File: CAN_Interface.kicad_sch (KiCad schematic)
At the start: 16 parts, among them CN2 BM04B-ACHSS, U1 TPSM82903, U2 TPS2117DRL, U7 TCAN1057AVDRBRQ1

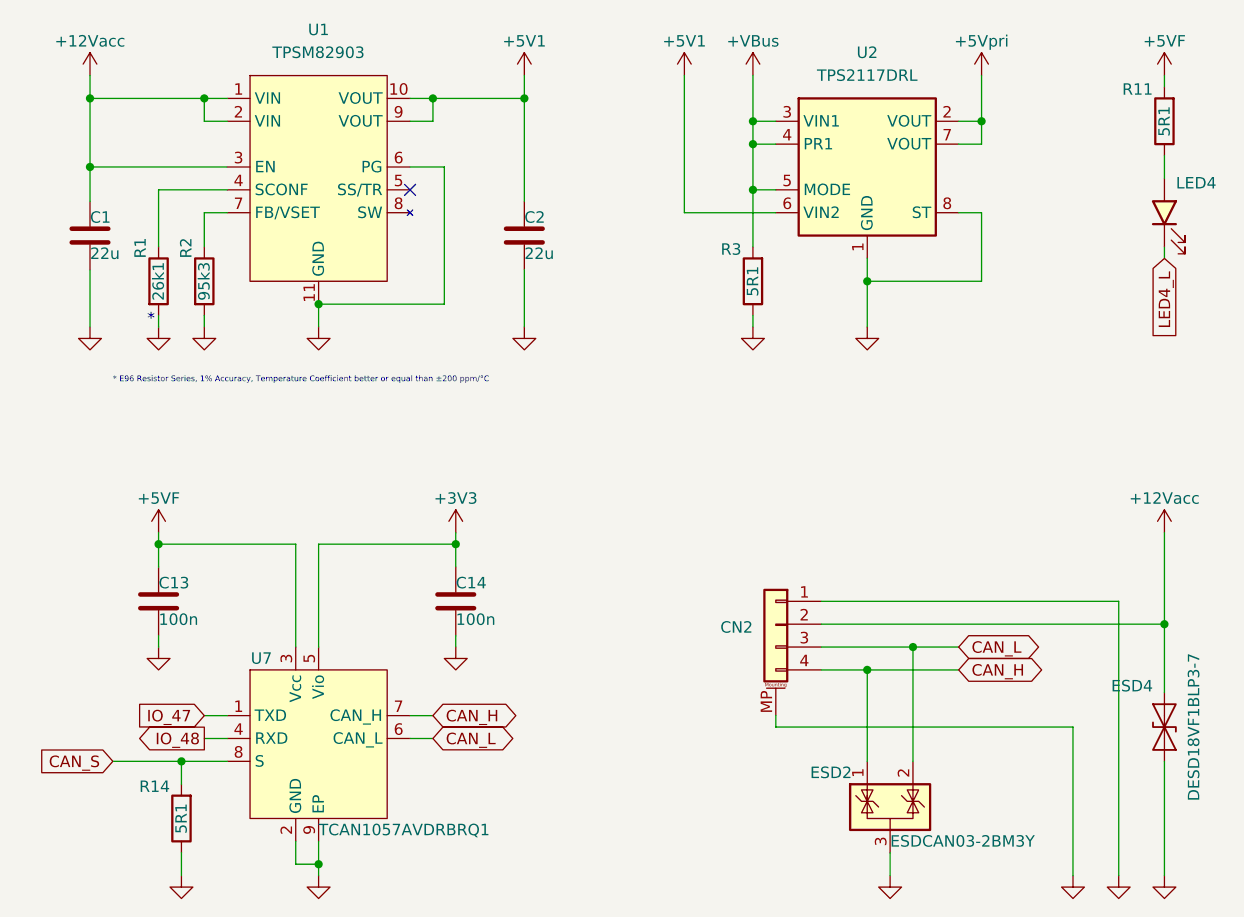
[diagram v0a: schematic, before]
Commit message: successful 1st pass, but I want to try some new bus'ing techniques to clean up the routing
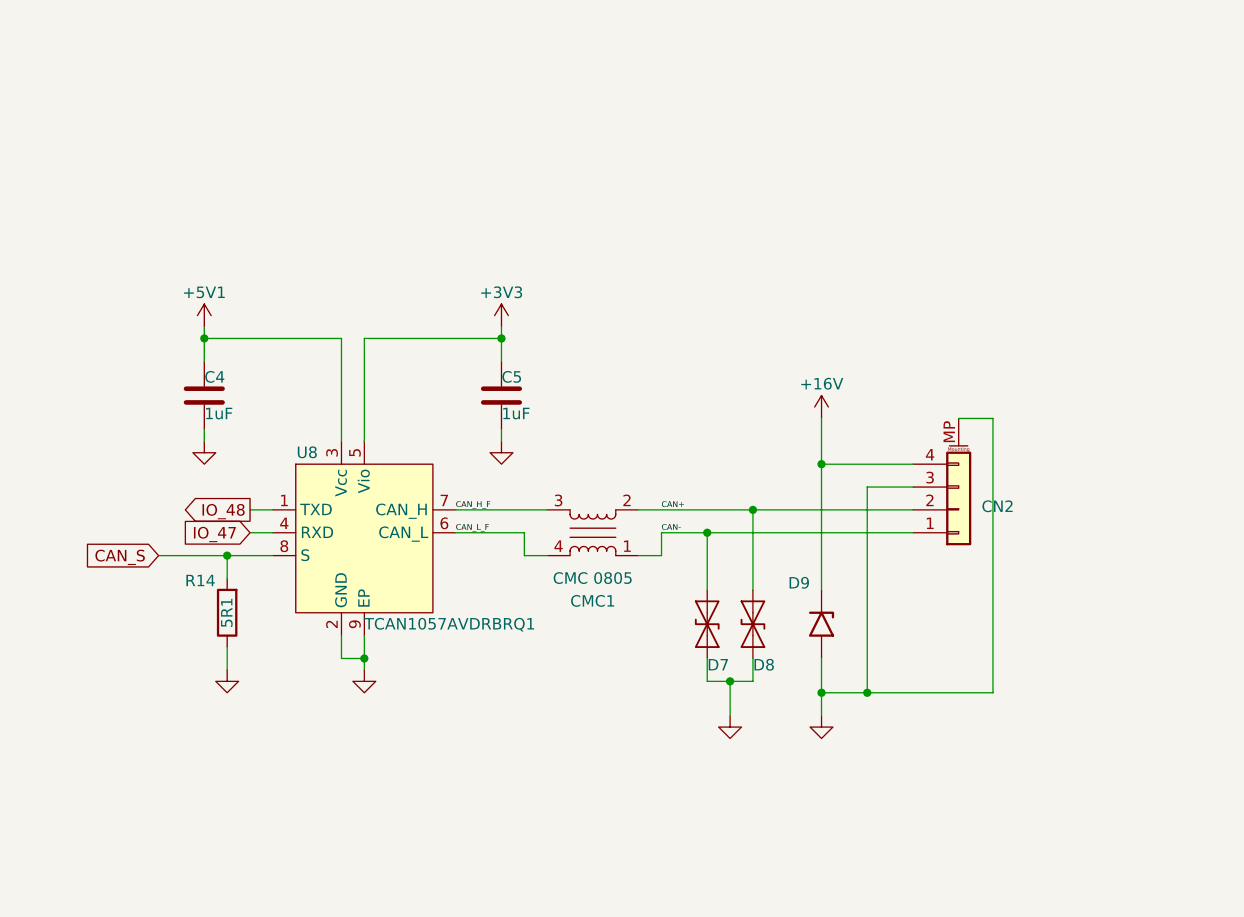
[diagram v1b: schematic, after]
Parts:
- removed C1, C2: 22u, Capacitors:C0805_Dense, symbol Device:C
- removed C13, C14: 100n, Capacitors:C0201_Dense, symbol Device:C
- removed ESD2: ESDCAN03-2BM3Y, Personal_FootprintLibrary:DFN1110-3, symbol PersonalSchematicSymbolLibrary:ESDCAN03-2BM3Y
- removed ESD4: DESD18VF1BLP3-7, Personal_FootprintLibrary:DSN0603-2, symbol PersonalSchematicSymbolLibrary:PESD5V0X1BCSF
- removed LED4: Red, Personal_FootprintLibrary:LED_0201-2, symbol PersonalSchematicSymbolLibrary:LED_Red
- removed R1: 26k1, Resistors:R0201_Nominal, symbol Device:R
- removed R11, R3: 5R1, Resistors:R0201_Nominal, symbol Device:R
- removed R2: 95k3, Resistors:R0201_Nominal, symbol Device:R
- removed U1: TPSM82903, Personal_FootprintLibrary:uSIP-11_3.0x2.8, symbol PersonalSchematicSymbolLibrary:TPSM82903
- removed U2: TPS2117DRL, Personal_FootprintLibrary:SOT5x3, symbol PersonalSchematicSymbolLibrary:TPS2117DRL
- added C4, C5: 1uF, Capacitors:C0201_Dense, symbol Device:C
- added CMC1: CMC 0805, Personal_FootprintLibrary:CMC_0805, symbol PersonalSchematicSymbolLibrary:Choke_CommonMode_TDK_ACM0805
- added D7, D8: PESD24VF1BL-Q, Personal_FootprintLibrary:DFN1006-2, symbol PersonalSchematicSymbolLibrary:PESD24VF1BBL-Q
- added D9: VESD16C1-HD1HG3-08, Personal_FootprintLibrary:DFN1006-2, symbol PersonalSchematicSymbolLibrary:TVS_Unidirectional
- R14: footprint Resistors:R0201_Nominal -> Resistors:R0201_Dense
- renumbered U7 to U8
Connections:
- net +5VF is gone; now on net +5V1: U8.3 (Vcc)
- net +3V3: now also C5.1
- net +5V1: now also C4.1
- net GND: now also CN2.3 (CAN_L), C4.2, C5.2, D7.2 (A2), D8.2 (A2), D9.2 (A2); no longer CN2.1 (GND)
- net IO_47: now also U8.4 (RXD); no longer U8.1 (TXD)
- net IO_48: now also U8.1 (TXD); no longer U8.4 (RXD)
- net +12Vacc renamed CAN+
- net CAN+: now also CMC1.2, D8.1 (A1)
- net CAN_H renamed +16V
- net +16V: now also D9.1 (A1); no longer U8.7 (CAN_H)
- net CAN_L renamed CAN_L_F
- net CAN_L_F: now also CMC1.4; no longer CN2.3 (CAN_L)
- new net CAN-: CMC1.1, CN2.1 (GND), D7.1 (A1)
- new net CAN_H_F: CMC1.3, U8.7 (CAN_H)
- no-connect marks 1 -> 0
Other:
- note removed: "*"
- note removed: "* E96 Resistor Series, 1% Accuracy, Temperature Coefficient better or equal than ±200 ppm/°C"
- moved on the sheet: CN2, R14, U8

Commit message: Update CAN_Interface.kicad_sch, ESP32-S3 Pico D1.kicad_dru, ESP32-S3 Pico D1.kicad_pcb, and 5 more files reroute completed
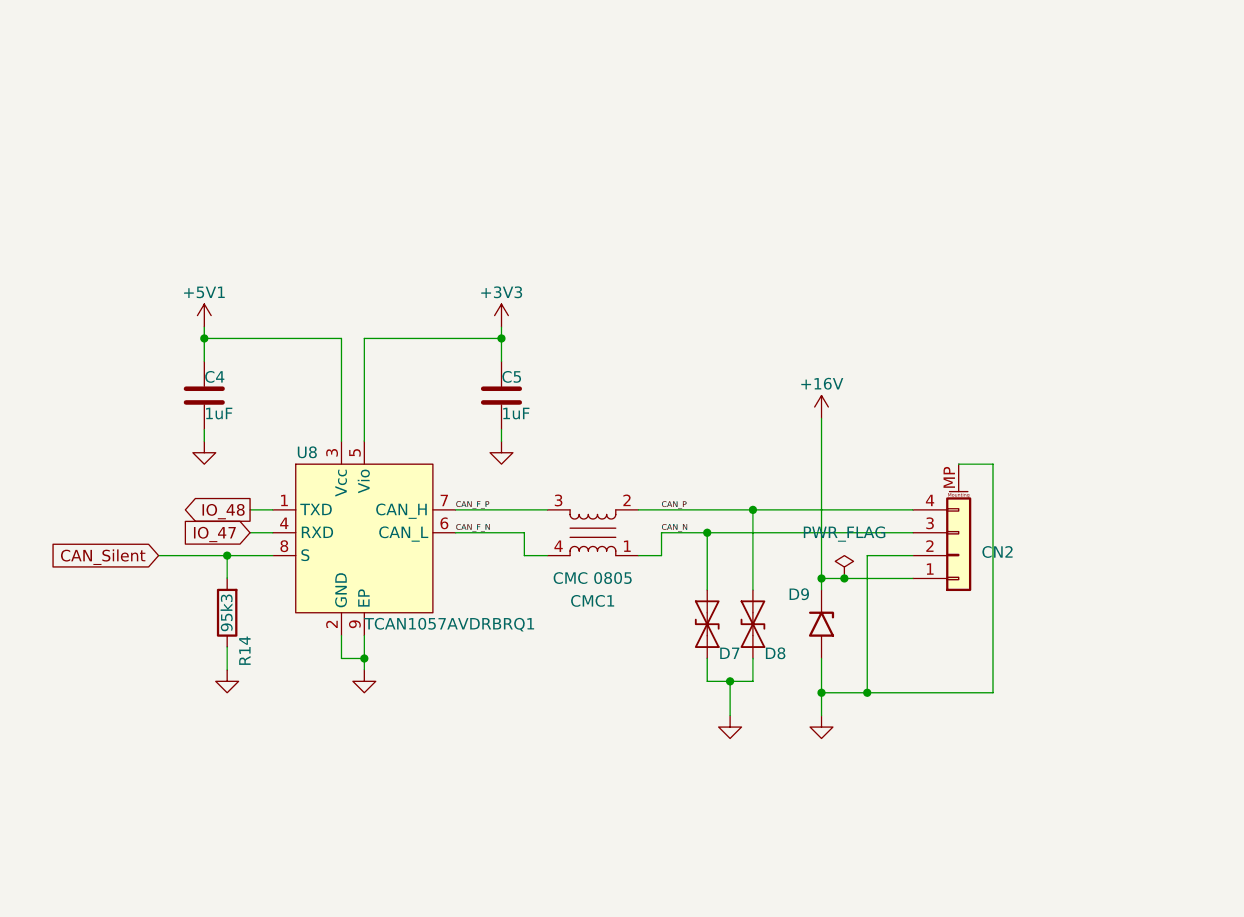
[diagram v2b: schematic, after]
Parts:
- CN2: LCSC C46772640, C5246838, C5308725 -> C46772640; Manufacturer JST -> XUNPU; Manufacturer (alt) Xunpu -> (none); Manufacturer Part Number BM04B-ACHSS-A-GAN-TF(LF)(SN), BM04B-ACHSS-A-GAN-ETF(LF)(SN) -> WAFER-ACH1.2-4PWB; Manufacturer Part Number (alt) WAFER-ACH1.2-4PWB -> (none)
- D7, D8: value PESD24VF1BL-Q -> ESDSLC24VLB-TP; Distributor Link 1 https://www.digikey.com/en/products/detail/nexperia-usa-inc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 -> https://www.digikey.com/en/products/detail/mcc-micro-commer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; Distributor Link 2 https://www.mouser.com/ProductDetail/Nexperia/PESD24VF1BBL-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 -> https://www.mouser.com/ProductDetail/Micro-Commercial-Compo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; LCSC C22465859 -> C7463931; Manufacturer Nexperia -> MCC(Micro Commercial Components); Manufacturer Part Number PESD24VF1BBL-Q -> ESDSLC24VLB-TP
- D9: value VESD16C1-HD1HG3-08 -> D15V0H1U2LP-7B; Distributor Link 1 https://www.digikey.com/en/products/detail/vishay-general-s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 -> https://www.digikey.com/en/products/detail/diodes-incorpora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; Distributor Link 2 https://www.mouser.com/ProductDetail/Vishay-General-Semicon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 -> https://www.mouser.com/ProductDetail/Diodes-Incorporated/D1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; LCSC C3703781 -> C1973850; Manufacturer Vishay -> Diodes Incorporated; Manufacturer Part Number VESD16C1-HD1HG3-08 -> D15V0H1U2LP-7B
- R14: value 5R1 -> 95k3; Distributor Link 2 https://www.mouser.com/ProductDetail/Royalohm/PF01WMF5100TE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 -> https://www.mouser.com/ProductDetail/Royalohm/0201WMF9532TE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; LCSC C50670526 -> C423395; Manufacturer Part Number PF01WMF510KTEE -> 0201WMF9532TEE
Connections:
- net +16V: now also CN2.1 (GND); no longer CN2.4 (CAN_H)
- net GND: now also CN2.2 (+12V); no longer CN2.3 (CAN_L)
- net CAN+ renamed CAN_P
- net CAN_P: now also CN2.4 (CAN_H); no longer CN2.2 (+12V)
- net CAN- renamed CAN_N
- net CAN_N: now also CN2.3 (CAN_L); no longer CN2.1 (GND)
- net CAN_H_F renamed CAN_F_P
- net CAN_L_F renamed CAN_F_N
- net CAN_S renamed CAN_Silent
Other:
- moved on the sheet: CN2
